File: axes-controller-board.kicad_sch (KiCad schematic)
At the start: 53 parts, among them IC1 TPS5450QDDARQ1, J10 Conn_01x08, J11 Conn_01x04, J12 Conn_01x08, J13 Conn_01x04, J14 Conn_01x08, J15 Conn_01x08, J16 Conn_01x04, J17 Conn_01x08, J18 Conn_01x08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

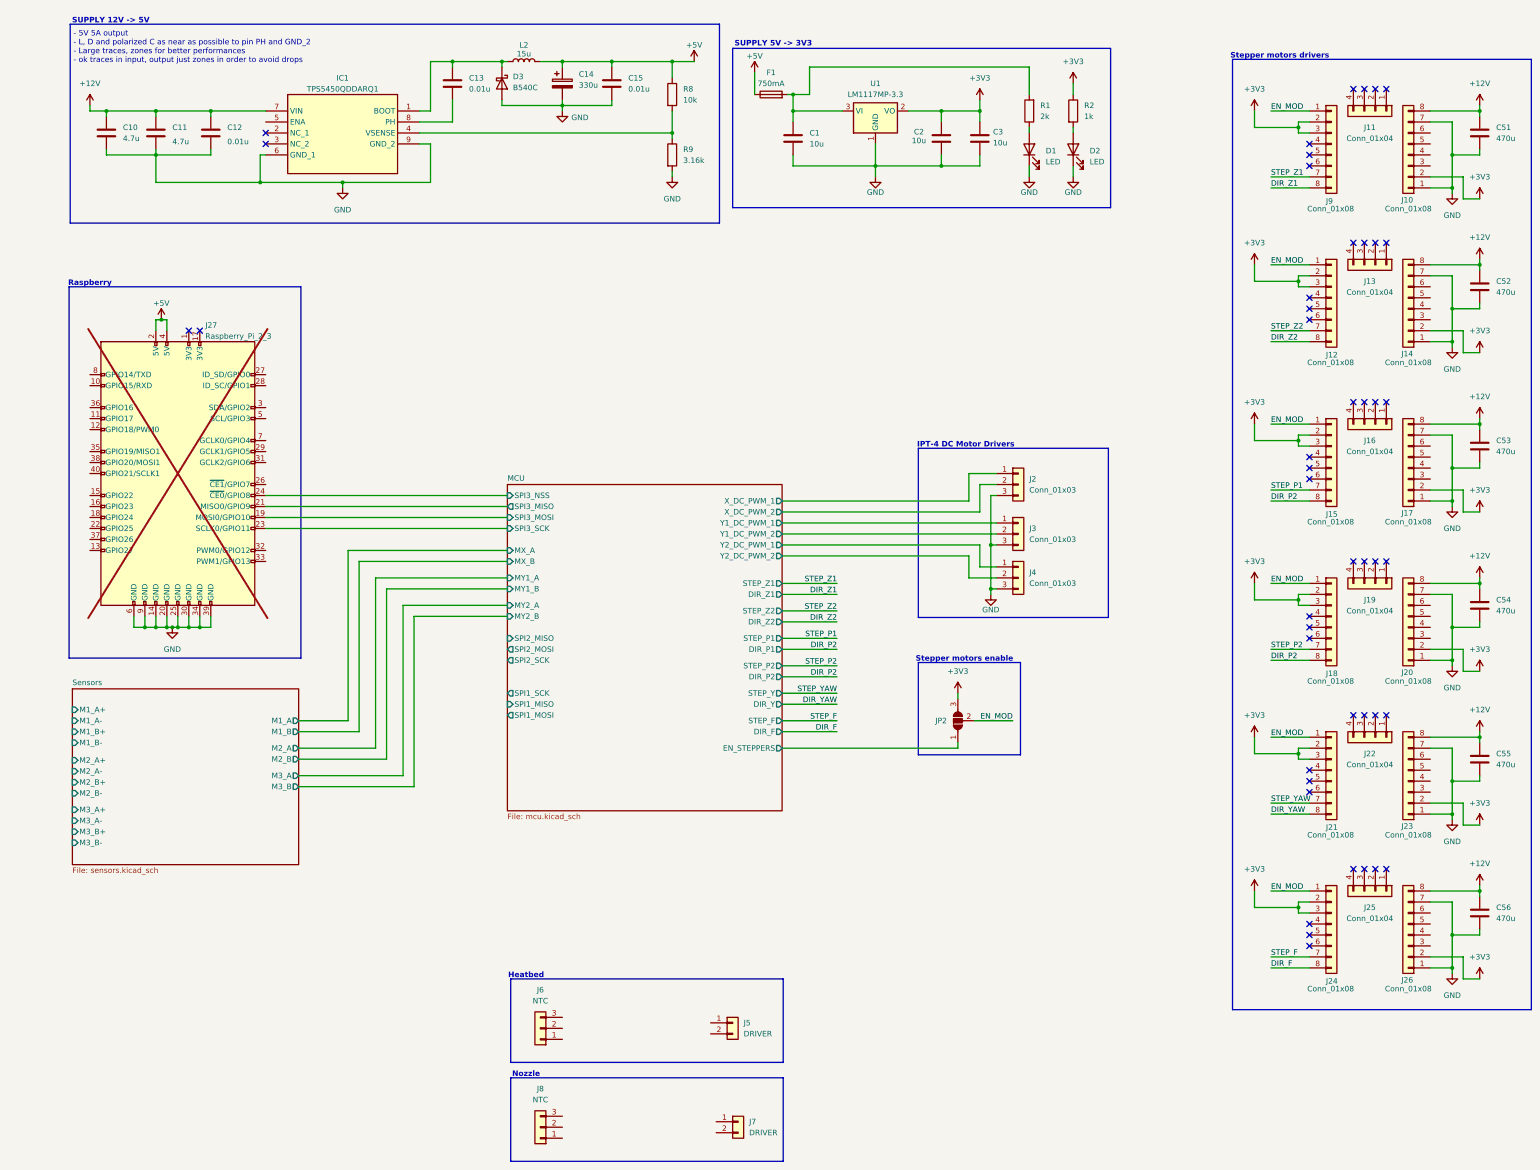
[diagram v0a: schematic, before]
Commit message: fix: missing footprints and new current sensor
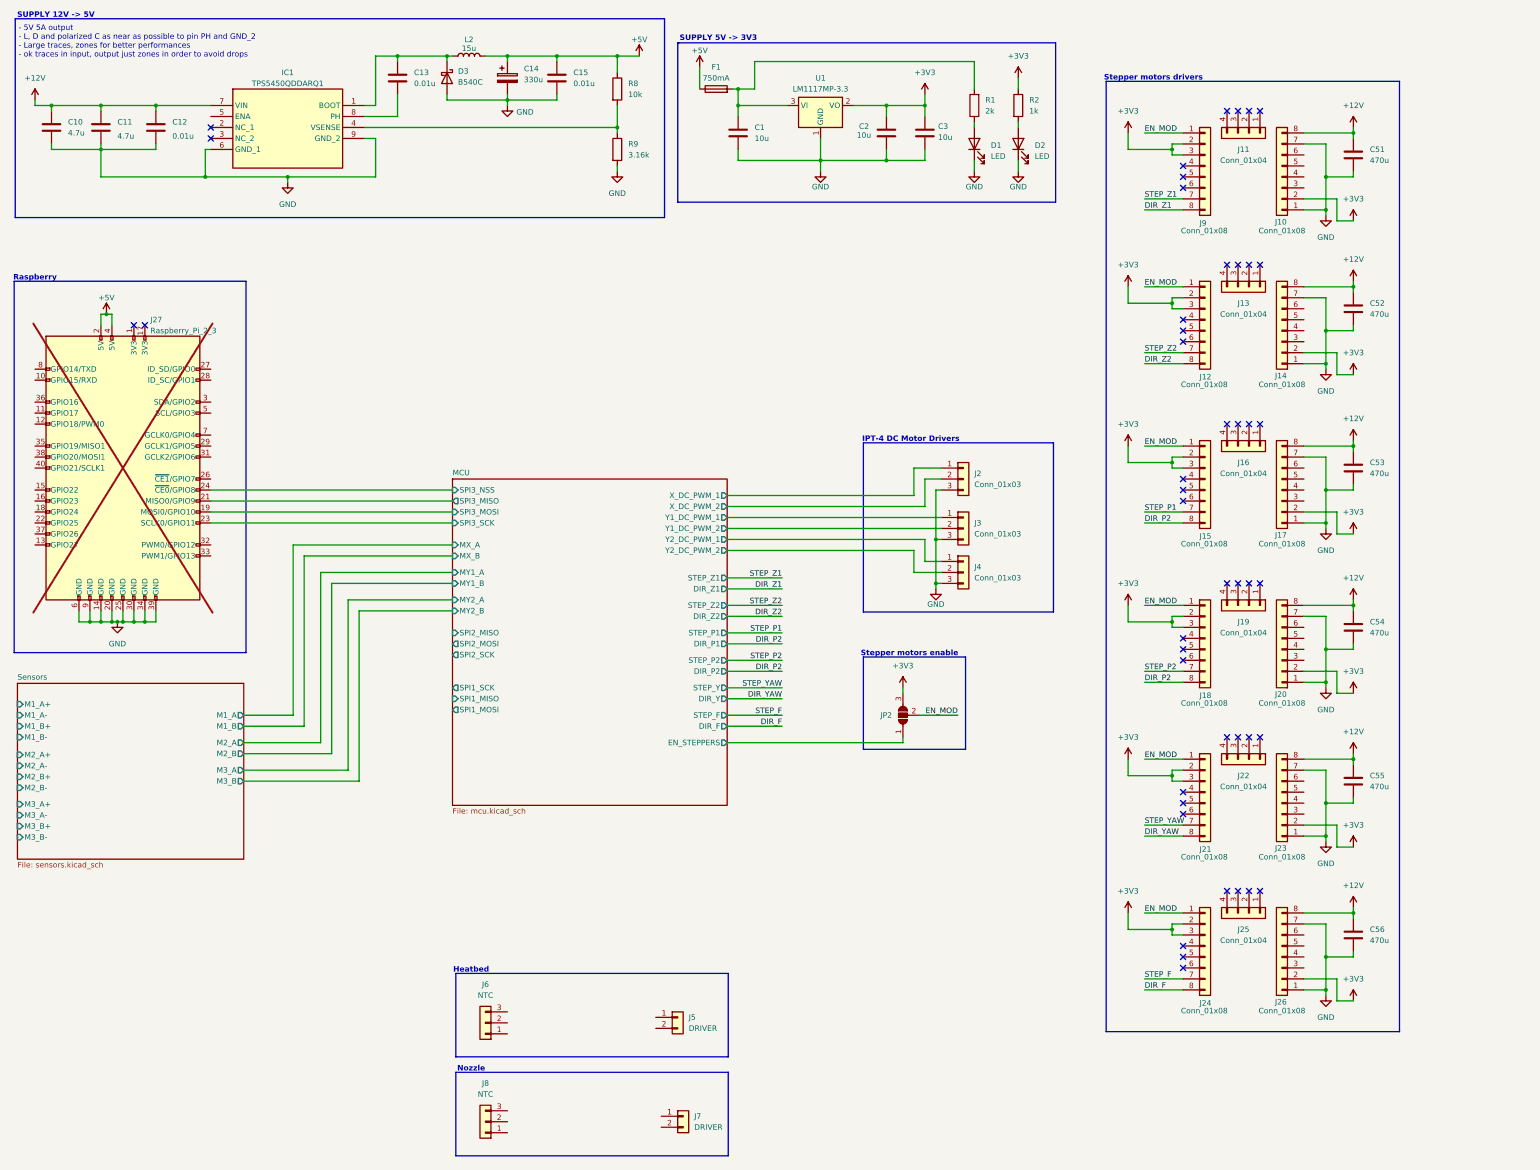
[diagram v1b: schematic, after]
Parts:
- C10, C11: footprint (none) -> Capacitor_SMD:C_0805_2012Metric
- C12, C13, C15: footprint (none) -> Capacitor_SMD:C_0603_1608Metric
- C14: footprint (none) -> Capacitor_THT:CP_Radial_D10.0mm_P5.00mm
- D3: footprint (none) -> Diode_SMD:D_SMC_Handsoldering
- IC1: footprint SOIC127P600X170-9N -> Local:SOIC127P600X170-9N
- J2, J3, J4, J6, J8: footprint (none) -> Connector_PinHeader_2.54mm:PinHeader_1x03_P2.54mm_Vertical
- J5, J7: footprint (none) -> Connector_PinHeader_2.54mm:PinHeader_1x02_P2.54mm_Vertical
- L2: footprint (none) -> Inductor_SMD:L_12x12mm_H6mm
- R8, R9: footprint (none) -> Resistor_SMD:R_0603_1608Metric
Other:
- moved on the sheet: C1, C10, C11, C12, C13, C14, C15, C2, C3, C51, C52, C53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

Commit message: fix: minors
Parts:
- added J28: DC1, Connector_PinHeader_2.54mm:PinHeader_1x02_P2.54mm_Vertical, symbol Connector_Generic:Conn_01x02
- added J29: DC2, Connector_PinHeader_2.54mm:PinHeader_1x02_P2.54mm_Vertical, symbol Connector_Generic:Conn_01x02
- added J30: DC3, Connector_PinHeader_2.54mm:PinHeader_1x02_P2.54mm_Vertical, symbol Connector_Generic:Conn_01x02
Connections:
- new net Sensors/DC_1_IN: J28.2 (Pin_2)
- new net Sensors/DC_1_OUT: J28.1 (Pin_1)
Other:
- sheet MCU ports: added SPI4_MISO, SPI4_MOSI, SPI4_SCK; removed none
- sheet Sensors ports: added DC_1_IN, DC_1_OUT; removed none
- moved on the sheet: J27

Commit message: feat: rotative encoders connectors setup
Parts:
- added J31, J32: Conn_01x08, Connector_PinHeader_2.54mm:PinHeader_1x08_P2.54mm_Vertical, symbol Connector_Generic:Conn_01x08
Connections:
- net +3V3: now also J31.1 (Pin_1), J31.2 (Pin_2), J32.1 (Pin_1), J32.2 (Pin_2)
- net GND: now also J31.8 (Pin_8), J32.8 (Pin_8)
- net MCU/SPI1_MISO: now also J32.7 (Pin_7)
- net MCU/SPI1_MOSI: now also J32.6 (Pin_6)
- net MCU/SPI1_SCK: now also J32.5 (Pin_5)
- net MCU/SPI2_MISO: now also J31.7 (Pin_7)
- net MCU/SPI2_MOSI: now also J31.6 (Pin_6)
- net MCU/SPI2_SCK: now also J31.5 (Pin_5)
- new net MCU/SPI1_NSS: J31.4 (Pin_4)
- new net MCU/SPI2_NSS: J32.4 (Pin_4)
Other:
- sheet MCU ports: added SPI1_NSS, SPI2_NSS; removed none
- note added: "HEADERS"
- note added: "Rotative Encoders"
- moved on the sheet: C1, C10, C11, C12, C13, C14, C15, C2, C3, C51, C52, C53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

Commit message: feat: current sensor setup
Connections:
- net Sensors/DC_3_OUT: now reaches J30.1 (Pin_1)
- net Sensors/DC_3_IN: now reaches J30.2 (Pin_2)
- net Sensors/DC_2_OUT: now reaches J29.1 (Pin_1)
- net Sensors/DC_2_IN: now reaches J29.2 (Pin_2)
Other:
- sheet MCU ports: added SPI4_CSS_X, SPI4_CSS_Y1, SPI4_CSS_Y2; removed none
- sheet Sensors ports: added DC_2_IN, DC_2_OUT, DC_3_IN, DC_3_OUT, SPI4_CSS_X, SPI4_CSS_Y1, SPI4_CSS_Y2, SPI4_MISO, SPI4_MOSI, SPI4_SCK; removed none
- note added: "Just for current reading"
- note added: "Power terminals"
- moved on the sheet: J27, J28, J29, J30, J31, J32

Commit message: fix: chip selects
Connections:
- net MCU/SPI1_NSS renamed MCU/SPI2_CSS
- net MCU/SPI2_NSS renamed MCU/SPI1_CSS
- net MCU/SPI3_NSS renamed MCU/SPI3_CSS
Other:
- sheet MCU ports: added SPI1_CSS, SPI2_CSS, SPI3_CSS; removed SPI1_NSS, SPI2_NSS, SPI3_NSS
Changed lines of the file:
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@@
 	)
 	(sheet
-		(at 265.43 149.86)
-		(size 63.5 99.822)
+		(at 265.43 145.796)
+		(size 63.5 103.886)
 		(fields_autoplaced yes)
 		(stroke
@@
 		)
 		(property "Sheetname" "MCU"
-			(at 265.43 149.1484 0)
+			(at 265.43 145.0844 0)
 			(effects
 				(font
@@
 			)
 		)
-		(pin "SPI3_NSS" input
-			(at 265.43 154.94 180)
-			(effects
-				(font
-					(size 1.27 1.27)
-				)
-				(justify left)
-			)
-		)
 		(pin "SPI3_SCK" input
 			(at 265.43 162.56 180)
@@
 			)
 		)
-		(pin "SPI1_NSS" output
-			(at 265.43 228.6 180)
-			(effects
-				(font
-					(size 1.27 1.27)
-				)
-				(justify left)
-			)
-		)
-		(pin "SPI2_NSS" output
-			(at 265.43 213.36 180)
-			(effects
-				(font
-					(size 1.27 1.27)
-				)
-				(justify left)
-			)
-		)
 		(pin "SPI4_CSS_Y2" output
 			(at 265.43 205.74 180)
@@
 			(effects
 				(font
+					(size 1.27 1.27)
+				)
+				(justify left)
+			)
+		)
+		(pin "SPI2_CSS" output
+			(at 265.43 228.6 180)
+			(effects
+				(font
+					(size 1.27 1.27)
+				)
+				(justify left)
+			)
+		)
+		(pin "SPI1_CSS" output
+			(at 265.43 213.36 180)
+			(effects
+				(font
+					(size 1.27 1.27)
+				)
+				(justify left)
+			)
+		)
+		(pin "SPI3_CSS" output
+			(at 265.43 154.94 180)
+			(effects
+				(font

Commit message: feat: setup micro on pcb
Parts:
- J28, J29, J30: footprint Connector_PinHeader_2.54mm:PinHeader_1x02_P2.54mm_Vertical -> TerminalBlock_Phoenix:TerminalBlock_Phoenix_MKDS-1,5-2-5.08_1x02_P5.08mm_Horizontal
- J31, J32: footprint Connector_PinHeader_2.54mm:PinHeader_1x08_P2.54mm_Vertical -> Connector_Molex:Molex_Micro-Fit_3.0_43045-0812_2x04_P3.00mm_Vertical
- JP2: footprint (none) -> Jumper:SolderJumper-3_P1.3mm_Open_RoundedPad1.0x1.5mm
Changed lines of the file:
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@@
 			)
 		)
-		(property "Footprint" "Connector_PinHeader_2.54mm:PinHeader_1x02_P2.54mm_Vertical"
+		(property "Footprint" "TerminalBlock_Phoenix:TerminalBlock_Phoenix_MKDS-1,5-2-5.08_1x02_P5.08mm_Horizontal"
 			(at 74.93 242.57 0)
 			(effects
@@
 			)
 		)
-		(property "Footprint" "Connector_PinHeader_2.54mm:PinHeader_1x02_P2.54mm_Vertical"
+		(property "Footprint" "TerminalBlock_Phoenix:TerminalBlock_Phoenix_MKDS-1,5-2-5.08_1x02_P5.08mm_Horizontal"
 			(at 74.93 257.81 0)
 			(effects
@@
 			)
 		)
-		(property "Footprint" ""
+		(property "Footprint" "Jumper:SolderJumper-3_P1.3mm_Open_RoundedPad1.0x1.5mm"
 			(at 373.38 224.79 0)
 			(effects
@@
 			)
 		)
-		(property "Footprint" "Connector_PinHeader_2.54mm:PinHeader_1x08_P2.54mm_Vertical"
+		(property "Footprint" "Connector_Molex:Molex_Micro-Fit_3.0_43045-0812_2x04_P3.00mm_Vertical"
 			(at 132.08 294.64 0)
 			(effects
@@
 			)
 		)
-		(property "Footprint" "Connector_PinHeader_2.54mm:PinHeader_1x08_P2.54mm_Vertical"
+		(property "Footprint" "Connector_Molex:Molex_Micro-Fit_3.0_43045-0812_2x04_P3.00mm_Vertical"
 			(at 132.08 328.93 0)
 			(effects
@@
 			)
 		)
-		(property "Footprint" "Connector_PinHeader_2.54mm:PinHeader_1x02_P2.54mm_Vertical"
+		(property "Footprint" "TerminalBlock_Phoenix:TerminalBlock_Phoenix_MKDS-1,5-2-5.08_1x02_P5.08mm_Horizontal"
 			(at 74.93 250.19 0)
 			(effects

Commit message: feat: setup groups pcb
steppers, micro, clock, current sensor - connector
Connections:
- net +12V: now also J10.1 (Pin_1), J14.1 (Pin_1), J17.1 (Pin_1), J20.1 (Pin_1), J23.1 (Pin_1), J26.1 (Pin_1); no longer J10.8 (Pin_8), J14.8 (Pin_8), J17.8 (Pin_8), J20.8 (Pin_8), J23.8 (Pin_8), J26.8 (Pin_8)
- net +3V3: now also J10.7 (Pin_7), J14.7 (Pin_7), J17.7 (Pin_7), J20.7 (Pin_7), J23.7 (Pin_7), J26.7 (Pin_7); no longer J10.2 (Pin_2), J14.2 (Pin_2), J17.2 (Pin_2), J20.2 (Pin_2), J23.2 (Pin_2), J26.2 (Pin_2)
- net GND: now also J10.2 (Pin_2), J10.8 (Pin_8), J14.2 (Pin_2), J14.8 (Pin_8), J17.2 (Pin_2), J17.8 (Pin_8), J20.2 (Pin_2), J20.8 (Pin_8), J23.2 (Pin_2), J23.8 (Pin_8), J26.2 (Pin_2), J26.8 (Pin_8); no longer J10.1 (Pin_1), J10.7 (Pin_7), J14.1 (Pin_1), J14.7 (Pin_7), J17.1 (Pin_1), J17.7 (Pin_7), J20.1 (Pin_1), J20.7 (Pin_7), J23.1 (Pin_1), J23.7 (Pin_7), J26.1 (Pin_1), J26.7 (Pin_7)
- net Sensors/DC_1_IN: now also J28.1 (Pin_1); no longer J28.2 (Pin_2)
- net Sensors/DC_1_OUT: now also J28.2 (Pin_2); no longer J28.1 (Pin_1)
- net Sensors/DC_2_IN: now also J29.1 (Pin_1); no longer J29.2 (Pin_2)
- net Sensors/DC_2_OUT: now also J29.2 (Pin_2); no longer J29.1 (Pin_1)
- net Sensors/DC_3_IN: now also J30.1 (Pin_1); no longer J30.2 (Pin_2)
- net Sensors/DC_3_OUT: now also J30.2 (Pin_2); no longer J30.1 (Pin_1)
- net IBC: now reaches C13.1, IC1.8 (PH)
- net IBC: now also D3.1 (K), L2.1
- net at C13.2, IC1.1 (BOOT): no longer D3.1 (K), L2.1
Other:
- moved on the sheet: J10, J14, J17, J20, J23, J26, J28, J29, J30

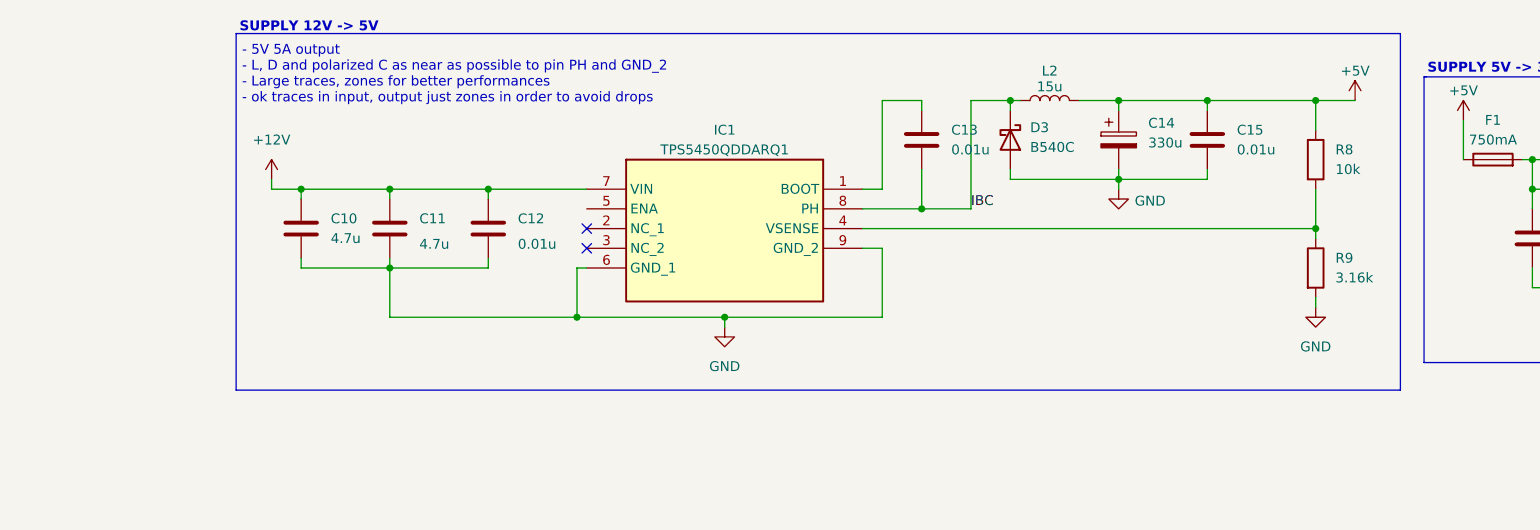
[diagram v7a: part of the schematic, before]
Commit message: fix: missing input power connector
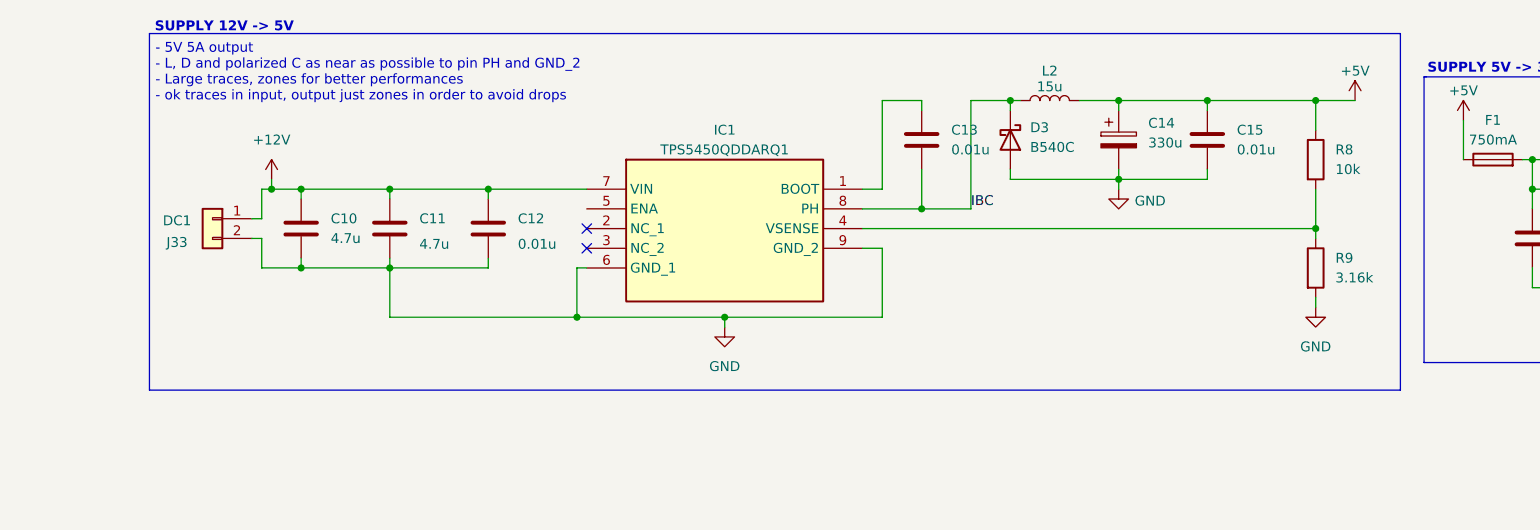
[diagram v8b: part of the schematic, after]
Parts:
- added J33: DC1, TerminalBlock_Phoenix:TerminalBlock_Phoenix_MKDS-1,5-2-5.08_1x02_P5.08mm_Horizontal, symbol Connector_Generic:Conn_01x02
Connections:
- net +12V: now also J33.1 (Pin_1)
- net GND: now also J33.2 (Pin_2)
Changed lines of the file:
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@@
 	)
 	(junction
+		(at 170.18 71.12)
+		(diameter 0)
+		(color 0 0 0 0)
+	)
+	(junction
 		(at 328.93 57.15)
 		(diameter 0)
@@
 	)
 	(junction
+		(at 166.37 60.96)
+		(diameter 0)
+		(color 0 0 0 0)
+	)
+	(junction
 		(at 511.81 283.21)
 		(diameter 0)
@@
 	(wire
 		(pts
+			(xy 165.1 60.96) (xy 166.37 60.96)
+		)
+		(stroke
+			(width 0)
+			(type default)
+		)
+	)
+	(wire
+		(pts
 			(xy 421.64 172.72) (xy 421.64 184.15)
 		)
@@
 	(wire
 		(pts
+			(xy 163.83 67.31) (xy 165.1 67.31)
+		)
+		(stroke
+			(width 0)
+			(type default)
+		)
+	)
+	(wire
+		(pts
 			(xy 132.08 185.42) (xy 133.35 185.42)
 		)
@@
 	(wire
 		(pts
+			(xy 165.1 64.77) (xy 165.1 60.96)
+		)
+		(stroke
+			(width 0)
+			(type default)
+		)
+	)
+	(wire
+		(pts
 			(xy 242.57 328.93) (xy 242.57 228.6)
 		)
@@
 		)
 	)
+	(wire
+		(pts
+			(xy 165.1 71.12) (xy 170.18 71.12)
+		)
+		(stroke
+			(width 0)
+			(type default)
+		)
+	)
 	(polyline
 		(pts
@@
 	(polyline
 		(pts
-			(xy 161.798 40.894) (xy 161.798 86.868)
+			(xy 150.622 40.894) (xy 150.622 86.868)
 		)
 		(stroke
@@
 	(polyline
 		(pts
-			(xy 161.798 86.868) (xy 311.912 86.868)
+			(xy 150.622 86.868) (xy 311.912 86.868)
 		)
 		(stroke
@@
 	(wire
 		(pts
+			(xy 165.1 67.31) (xy 165.1 71.12)
+		)
+		(stroke
+			(width 0)
+			(type default)
+		)
+	)
+	(wire
+		(pts
 			(xy 466.09 265.43) (xy 466.09 269.24)
 		)
@@
 	(wire
 		(pts
+			(xy 163.83 64.77) (xy 165.1 64.77)
+		)
+		(stroke
+			(width 0)
+			(type default)
+		)
+	)
+	(wire
+		(pts
 			(xy 476.25 270.51) (xy 476.25 269.24)
 		)
@@
 	(polyline
 		(pts
-			(xy 161.798 40.894) (xy 311.912 40.894)
+			(xy 150.622 40.894) (xy 311.912 40.894)
 		)
 		(stroke
@@
 	(text "SUPPLY 12V -> 5V"
 		(exclude_from_sim no)
-		(at 171.196 40.132 0)
+		(at 160.274 40.132 0)
 		(effects
 			(font
@@
 	(text "- 5V 5A output\n- L, D and polarized C as near as possible to pin PH and GND_2\n- Large traces, zones for better performances\n- ok traces in input, output just zones in order to avoid drops"
 		(exclude_from_sim no)
-		(at 162.56 46.228 0)
+		(at 151.384 45.974 0)
 		(effects
 			(font
@@
 					(unit 1)
 				)
+			)
+		)
+	)
+	(symbol
+		(lib_id "Connector_Generic:Conn_01x02")
+		(at 158.75 64.77 0)
+		(mirror y)
+		(unit 1)
+		(exclude_from_sim no)
+		(in_bom yes)
+		(on_board yes)
+		(dnp no)
+		(property "Reference" "J33"
+			(at 154.178 67.818 0)
+			(effects
+				(font
+					(size 1.27 1.27)
+				)
+			)
+		)
+		(property "Value" "DC1"
+			(at 154.178 65.024 0)
+			(effects
+				(font
+					(size 1.27 1.27)
+				)
+			)
+		)
+		(property "Footprint" "TerminalBlock_Phoenix:TerminalBlock_Phoenix_MKDS-1,5-2-5.08_1x02_P5.08mm_Horizontal"
+			(at 158.75 64.77 0)
+			(effects
+				(font
+					(size 1.27 1.27)
+				)
+				(hide yes)
+			)
+		)
+		(property "Datasheet" "~"
+			(at 158.75 64.77 0)
+			(effects
+				(font
+					(size 1.27 1.27)
+				)
+				(hide yes)
+			)
+		)
+		(property "Description" "Generic connector, single row, 01x02, script generated (kicad-library-utils/schlib/autogen/connector/)"
+			(at 158.75 64.77 0)
+			(effects
+				(font
+					(size 1.27 1.27)
+				)
+				(hide yes)
+			)
+		)
+		(pin "1"
+		)
+		(pin "2"
+		)
+		(instances
+			(project "axes-controller-board"
+				(path "/88591975-6c45-4e1d-8f38-0b5760acfc98"
+					(reference "J33")
+					(unit 1)
+				)
